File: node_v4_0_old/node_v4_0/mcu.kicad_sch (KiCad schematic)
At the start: 27 parts, among them U1 RST, U4 RP2040, U5 BOOTSEL, U6 W25Q128JVS, Y1 445C35A12M00000

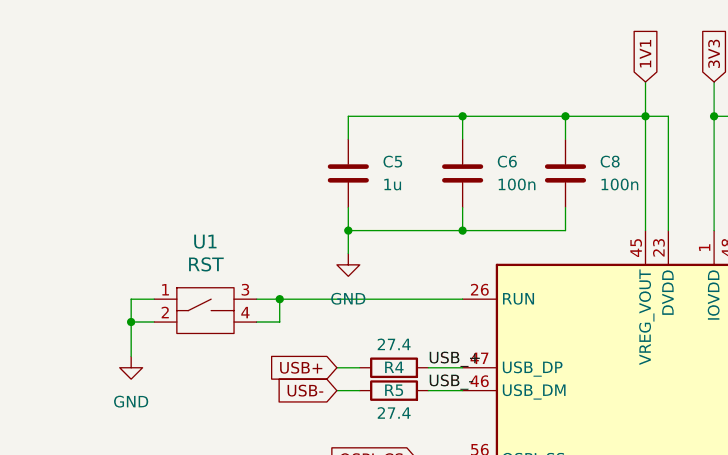
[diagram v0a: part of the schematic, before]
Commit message: converted v4 to different format and started the schematic(from scratch again)
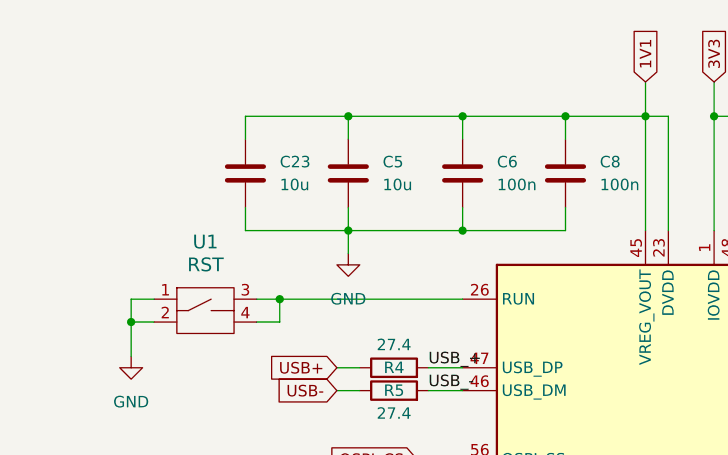
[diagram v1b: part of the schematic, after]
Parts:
- added C23: 10u, Capacitor_SMD:C_0805_2012Metric_Pad1.18x1.45mm_HandSolder, symbol Device:C
- C5: value 1u -> 10u
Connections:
- net 1V1: now also C23.1
- net GND: now also C23.2
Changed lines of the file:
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@@
 	)
 	(junction
+		(at 52.07 36.83)
+		(diameter 0)
+		(color 0 0 0 0)
+	)
+	(junction
 		(at 97.79 36.83)
 		(diameter 0)
@@
 	(wire
 		(pts
+			(xy 40.64 49.53) (xy 52.07 49.53)
+		)
+		(stroke
+			(width 0)
+			(type default)
+		)
+	)
+	(wire
+		(pts
 			(xy 100.33 36.83) (xy 130.81 36.83)
 		)
@@
 	(wire
 		(pts
+			(xy 40.64 36.83) (xy 52.07 36.83)
+		)
+		(stroke
+			(width 0)
+			(type default)
+		)
+	)
+	(wire
+		(pts
 			(xy 227.33 49.53) (xy 227.33 50.8)
 		)
@@
 	(wire
 		(pts
+			(xy 40.64 46.99) (xy 40.64 49.53)
+		)
+		(stroke
+			(width 0)
+			(type default)
+		)
+	)
+	(wire
+		(pts
 			(xy 115.57 85.09) (xy 118.11 85.09)
 		)
@@
 	(wire
 		(pts
+			(xy 40.64 39.37) (xy 40.64 36.83)
+		)
+		(stroke
+			(width 0)
+			(type default)
+		)
+	)
+	(wire
+		(pts
 			(xy 241.3 132.08) (xy 241.3 134.62)
 		)
@@
 			)
 		)
-		(property "Value" "1u"
+		(property "Value" "10u"
 			(at 55.88 44.45 0)
 			(effects
@@
 					(unit 1)
 				)
+			)
+		)
+	)
+	(symbol
+		(lib_id "Device:C")
+		(at 40.64 43.18 0)
+		(unit 1)
+		(exclude_from_sim no)
+		(in_bom yes)
+		(on_board yes)
+		(dnp no)
+		(property "Reference" "C23"
+			(at 44.45 41.91 0)
+			(effects
+				(font
+					(size 1.27 1.27)
+				)
+				(justify left)
+			)
+		)
+		(property "Value" "10u"
+			(at 44.45 44.45 0)
+			(effects
+				(font
+					(size 1.27 1.27)
+				)
+				(justify left)
+			)
+		)
+		(property "Footprint" "Capacitor_SMD:C_0805_2012Metric_Pad1.18x1.45mm_HandSolder"
+			(at 41.6052 46.99 0)
+			(effects
+				(font
+					(size 1.27 1.27)
+				)
+				(hide yes)
+			)
+		)
+		(property "Datasheet" "~"
+			(at 40.64 43.18 0)
+			(effects
+				(font
+					(size 1.27 1.27)
+				)
+				(hide yes)
+			)
+		)
+		(property "Description" ""
+			(at 40.64 43.18 0)
+			(effects
+				(font
+					(size 1.27 1.27)
+				)
+				(hide yes)
+			)
+		)
+		(pin "1"
+		)
+		(pin "2"
+		)
+		(instances
+			(project "node_v4_0"
+				(path "/28ed1f65-4a1b-4956-a97c-40b60632b5de/fedcb628-e44f-4ea0-9786-19abcc076df3"
+					(reference "C23")
+					(unit 1)
+				)
